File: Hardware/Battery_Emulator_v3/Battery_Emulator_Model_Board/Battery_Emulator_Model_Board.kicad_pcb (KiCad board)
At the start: 2 copper layers, 322.2 x 38.2 mm, 49 parts, among them J1 Vin, J10 Conn_01x05, J11 Conn_01x05, J12 Conn_01x05, J13 Conn_01x05, J14 Conn_01x05, J15 Conn_01x05, J16 Conn_01x05, J17 Conn_01x05, J2 USB4105-GF-A-060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

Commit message: Hardware update
Updated the size of the model board, so that it has 65mm of space for each cell board.
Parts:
- moved H4 137.8 mm to (481.9, 151.6)
- moved H3 137.8 mm to (481.9, 134.6)
- moved J11 137.8 mm to (487.6, 158.0)
- moved J3 137.8 mm to (497.8, 128.2)
- moved H6 118.1 mm to (415.0, 140.6)
- moved J10 118.1 mm to (432.9, 128.2)
- moved J17 118.1 mm to (422.7, 158.0)
- moved J9 98.8 mm to (367.9, 128.2)
- moved J16 98.8 mm to (357.8, 158.0)
- moved H8 80.2 mm to (286.0, 151.4)
- moved J8 80.2 mm to (303.0, 128.2)
- moved H7 80.2 mm to (286.0, 134.9)
- moved J15 80.2 mm to (292.8, 158.0)
- moved J14 62.8 mm to (227.9, 158.0)
- moved J7 62.8 mm to (238.1, 128.2)
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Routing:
- net +12V: track 693.3 -> 943.3 mm
- net +5V: track 683.1 -> 932.6 mm
- net /SCL: track 509.9 -> 634.7 mm
- net /SDA_cell_8-14: track 379.3 -> 486.9 mm
- net /SDA_cell_1-7: track 375.5 -> 479.5 mm
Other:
- board size 322.2 x 38.2 mm -> 446.7 x 38.2 mm

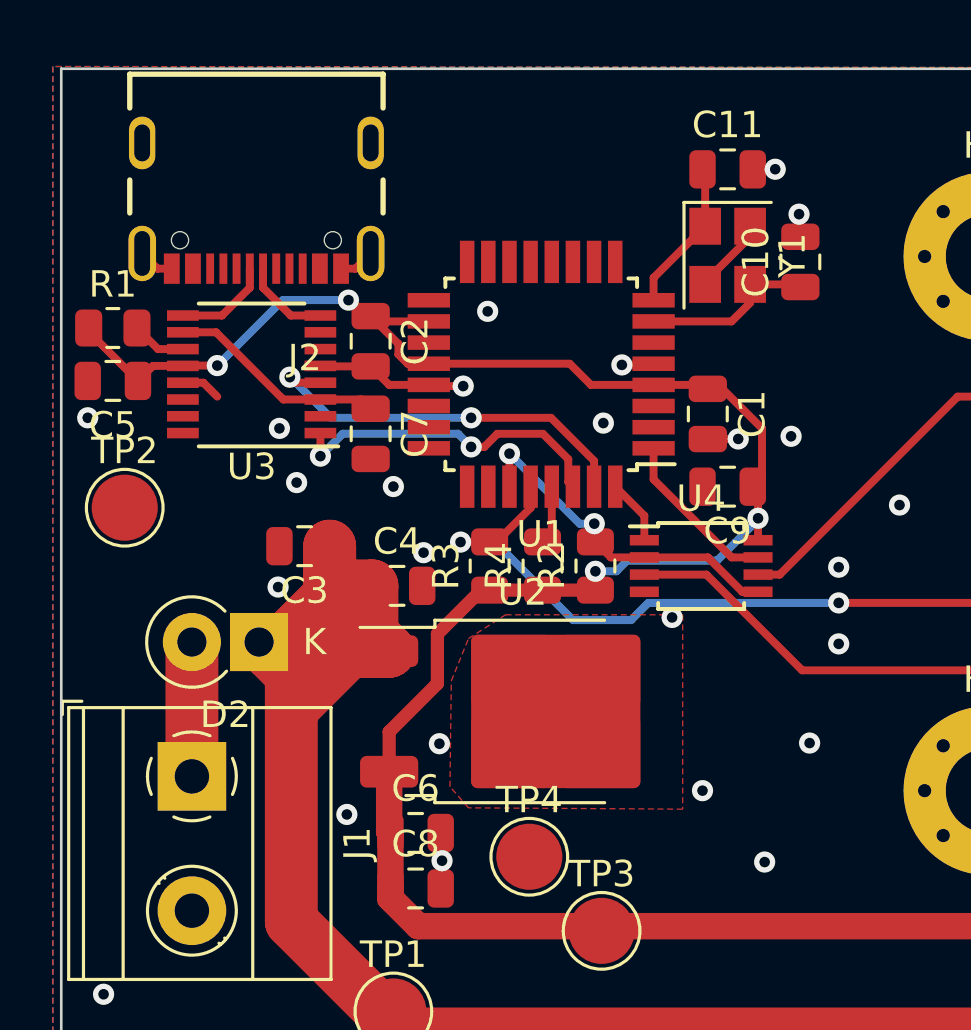
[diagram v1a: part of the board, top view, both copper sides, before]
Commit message: Hardware update
Moved some of the ground vias
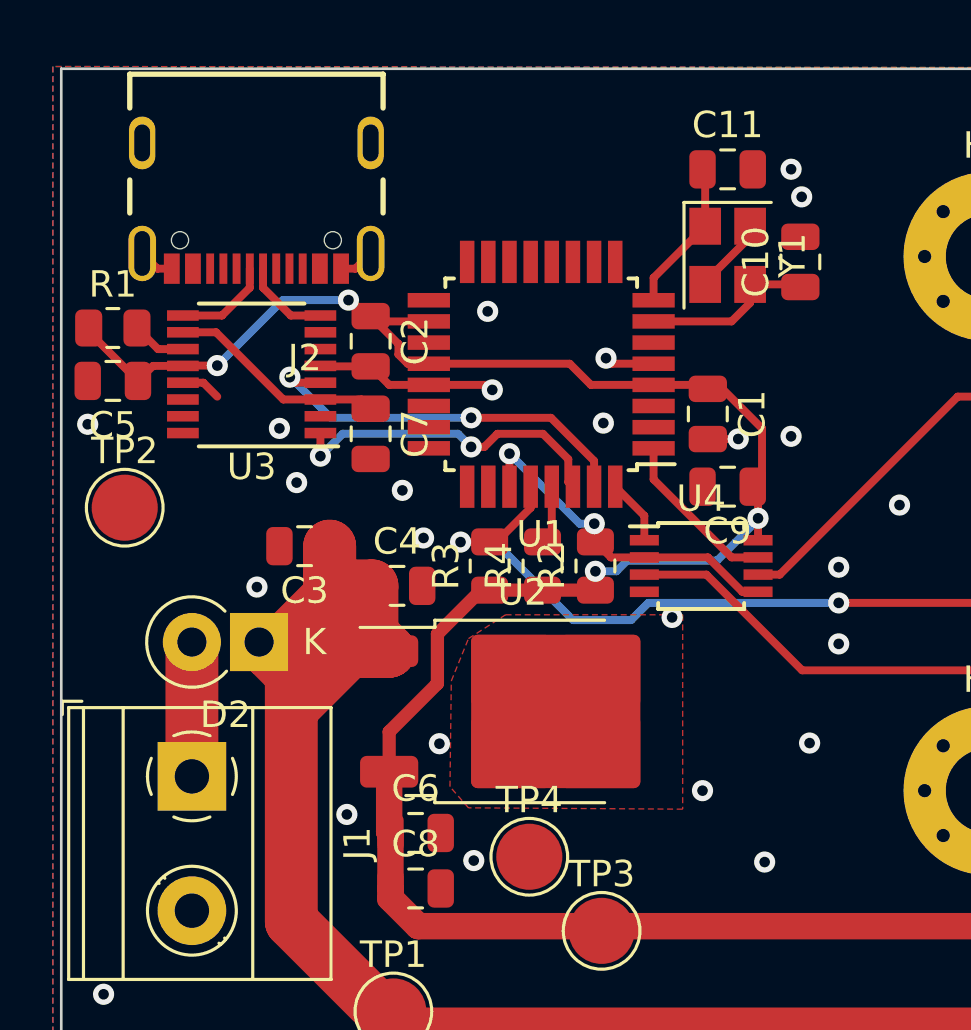
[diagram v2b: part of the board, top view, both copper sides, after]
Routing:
- net GND: track 15.2 -> 17.1 mm
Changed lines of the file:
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@@
   (segment (start 68.2 136.01025) (end 69.7 136.01025) (width 0.3) (layer "F.Cu") (net 2))
   (segment (start 66.38 131.61525) (end 66.925 131.61525) (width 0.3) (layer "F.Cu") (net 2))
-  (segment (start 77 135.25525) (end 78.155 135.25525) (width 0.3) (layer "F.Cu") (net 2))
   (segment (start 59.98 131.61525) (end 59.435 131.61525) (width 0.3) (layer "F.Cu") (net 2))
-  (segment (start 78.155 135.25525) (end 78.2 135.21025) (width 0.3) (layer "F.Cu") (net 2))
+  (segment (start 72.1 136.2) (end 71.91025 136.01025) (width 0.3) (layer "F.Cu") (net 2))
   (segment (start 81.85 130.415274) (end 81.85 130.01025) (width 0.3) (layer "F.Cu") (net 2))
   (segment (start 80.25 138.06025) (end 81.395 138.06025) (width 0.3) (layer "F.Cu") (net 2))
@@
   (segment (start 67.5 135.31025) (end 65.6175 135.31025) (width 0.3) (layer "F.Cu") (net 2))
   (segment (start 60.4 135.92775) (end 61.1725 135.92775) (width 0.3) (layer "F.Cu") (net 2))
+  (segment (start 76.61025 135.21025) (end 78.2 135.21025) (width 0.3) (layer "F.Cu") (net 2))
   (segment (start 65.6175 135.31025) (end 65.6 135.29275) (width 0.3) (layer "F.Cu") (net 2))
-  (segment (start 69.745 136.05525) (end 69.7 136.01025) (width 0.3) (layer "F.Cu") (net 2))
   (segment (start 81.395 138.06025) (end 81.4 138.05525) (width 0.3) (layer "F.Cu") (net 2))
+  (segment (start 71.91025 136.01025) (end 69.7 136.01025) (width 0.3) (layer "F.Cu") (net 2))
   (segment (start 80.15 132.21025) (end 80.15 132.115274) (width 0.3) (layer "F.Cu") (net 2))
-  (segment (start 71 136.05525) (end 69.745 136.05525) (width 0.3) (layer "F.Cu") (net 2))
   (segment (start 80.15 132.115274) (end 81.85 130.415274) (width 0.3) (layer "F.Cu") (net 2))
   (segment (start 66.925 131.61525) (end 67.5 131.04025) (width 0.3) (layer "F.Cu") (net 2))
+  (segment (start 76.4 135) (end 76.61025 135.21025) (width 0.3) (layer "F.Cu") (net 2))
   (segment (start 59.435 131.61525) (end 58.86 131.04025) (width 0.3) (layer "F.Cu") (net 2))
   (via (at 474.26 149.27525) (size 0.8) (drill 0.4) (layers "F.Cu" "B.Cu") (free) (net 2))
@@
   (via (at 472.71 147.22525) (size 0.8) (drill 0.4) (layers "F.Cu" "B.Cu") (free) (net 2))
   (via (at 430.31 133.62525) (size 0.8) (drill 0.4) (layers "F.Cu" "B.Cu") (free) (net 2))
-  (via (at 71 136.05525) (size 0.8) (drill 0.4) (layers "F.Cu" "B.Cu") (free) (net 2))
+  (via (at 72.1 136.2) (size 0.8) (drill 0.4) (layers "F.Cu" "B.Cu") (free) (net 2))
   (via (at 257.48 153.32525) (size 0.8) (drill 0.4) (layers "F.Cu" "B.Cu") (free) (net 2))
-  (via (at 56.8 137.25525) (size 0.8) (drill 0.4) (layers "F.Cu" "B.Cu") (free) (net 2))
+  (via (at 56.8 137.5) (size 0.8) (drill 0.4) (layers "F.Cu" "B.Cu") (free) (net 2))
   (via (at 421.51 139.02525) (size 0.8) (drill 0.4) (layers "F.Cu" "B.Cu") (free) (net 2))
   (via (at 109.6 137.70525) (size 0.8) (drill 0.4) (layers "F.Cu" "B.Cu") (free) (net 2))
@@
   (via (at 244.2 154.02525) (size 0.8) (drill 0.4) (layers "F.Cu" "B.Cu") (free) (net 2))
   (via (at 304.075 137.62525) (size 0.8) (drill 0.4) (layers "F.Cu" "B.Cu") (free) (net 2))
-  (via (at 77 135.25525) (size 0.8) (drill 0.4) (layers "F.Cu" "B.Cu") (free) (net 2))
+  (via (at 76.4 135) (size 0.8) (drill 0.4) (layers "F.Cu" "B.Cu") (free) (net 2))
   (via (at 125.4 158.05525) (size 0.8) (drill 0.4) (layers "F.Cu" "B.Cu") (free) (net 2))
   (via (at 474.425 142.53025) (size 0.8) (drill 0.4) (layers "F.Cu" "B.Cu") (free) (net 2))
@@
   (via (at 174.475 131.70275) (size 0.8) (drill 0.4) (layers "F.Cu" "B.Cu") (free) (net 2))
   (via (at 474.36 134.72525) (size 0.8) (drill 0.4) (layers "F.Cu" "B.Cu") (free) (net 2))
-  (via (at 70.2 154.00525) (size 0.8) (drill 0.4) (layers "F.Cu" "B.Cu") (free) (net 2))
+  (via (at 71.4 154) (size 0.8) (drill 0.4) (layers "F.Cu" "B.Cu") (free) (net 2))
   (via (at 117.4 139.05525) (size 0.8) (drill 0.4) (layers "F.Cu" "B.Cu") (free) (net 2))
   (via (at 383.2 158.02525) (size 0.8) (drill 0.4) (layers "F.Cu" "B.Cu") (free) (net 2))
@@
   (via (at 429.11 146.52525) (size 0.8) (drill 0.4) (layers "F.Cu" "B.Cu") (free) (net 2))
   (via (at 110 140.55525) (size 0.8) (drill 0.4) (layers "F.Cu" "B.Cu") (free) (net 2))
-  (via (at 68.36 139.85525) (size 0.8) (drill 0.4) (layers "F.Cu" "B.Cu") (free) (net 2))
+  (via (at 68.7 140) (size 0.8) (drill 0.4) (layers "F.Cu" "B.Cu") (free) (net 2))
   (via (at 364.2 146.72525) (size 0.8) (drill 0.4) (layers "F.Cu" "B.Cu") (free) (net 2))
   (via (at 70.1 149.58025) (size 0.8) (drill 0.4) (layers "F.Cu" "B.Cu") (free) (net 2))
@@
   (via (at 81.4 138.05525) (size 0.8) (drill 0.4) (layers "F.Cu" "B.Cu") (net 2))
   (via (at 421.41 150.22525) (size 0.8) (drill 0.4) (layers "F.Cu" "B.Cu") (free) (net 2))
-  (via (at 64 143.65525) (size 0.8) (drill 0.4) (layers "F.Cu" "B.Cu") (free) (net 2))
-  (via (at 69.5 142.35525) (size 0.8) (drill 0.4) (layers "F.Cu" "B.Cu") (free) (net 2))
+  (via (at 63.2 143.65525) (size 0.8) (drill 0.4) (layers "F.Cu" "B.Cu") (free) (net 2))
+  (via (at 69.5 141.8) (size 0.8) (drill 0.4) (layers "F.Cu" "B.Cu") (free) (net 2))
   (via (at 254 158.02525) (size 0.8) (drill 0.4) (layers "F.Cu" "B.Cu") (free) (net 2))
   (via (at 301.575 140.12525) (size 0.8) (drill 0.4) (layers "F.Cu" "B.Cu") (free) (net 2))
@@
   (via (at 87.5 140.55525) (size 0.8) (drill 0.4) (layers "F.Cu" "B.Cu") (free) (net 2))
   (via (at 280.075 139.02525) (size 0.8) (drill 0.4) (layers "F.Cu" "B.Cu") (free) (net 2))
-  (via (at 83.7 129.55525) (size 0.8) (drill 0.4) (layers "F.Cu" "B.Cu") (free) (net 2))
+  (via (at 83.8 128.9) (size 0.8) (drill 0.4) (layers "F.Cu" "B.Cu") (free) (net 2))
   (via (at 109.65 135.30525) (size 0.8) (drill 0.4) (layers "F.Cu" "B.Cu") (free) (net 2))
   (via (at 189.725 158.05275) (size 0.8) (drill 0.4) (layers "F.Cu" "B.Cu") (free) (net 2))
@@
   (via (at 80.05 151.35525) (size 0.8) (drill 0.4) (layers "F.Cu" "B.Cu") (free) (net 2))
   (via (at 320.675 128.22525) (size 0.8) (drill 0.4) (layers "F.Cu" "B.Cu") (free) (net 2))
-  (via (at 82.8 127.85525) (size 0.8) (drill 0.4) (layers "F.Cu" "B.Cu") (free) (net 2))
+  (via (at 83.4 127.85525) (size 0.8) (drill 0.4) (layers "F.Cu" "B.Cu") (free) (net 2))
   (via (at 385.8 154.02525) (size 0.8) (drill 0.4) (layers "F.Cu" "B.Cu") (free) (net 2))
   (via (at 104.8 154.23025) (size 0.8) (drill 0.4) (layers "F.Cu" "B.Cu") (free) (net 2))
